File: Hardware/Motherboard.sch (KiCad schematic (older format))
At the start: 1 part

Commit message: [Hardware] Added RTC battery and Adafruit BME680 board.
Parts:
- U1: renamed from U?; footprint (none) -> Package_SO:SOIC-28W_7.5x17.9mm_P1.27mm
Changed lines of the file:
@@
 EESchema Schematic File Version 4
+LIBS:Motherboard-cache
 EELAYER 30 0
 EELAYER END
@@
 $EndDescr
 $Comp
-L PIC18F23K22:PIC18F23K22 U?
+L PIC18F23K22:PIC18F23K22 U1
 U 1 1 5E7A8D16
 P 6300 3950
-F 0 "U?" H 6300 5320 50  0000 C CNN
+F 0 "U1" H 6300 5320 50  0000 C CNN
 F 1 "PIC18F23K22" H 6300 5229 50  0000 C CNN
-F 2 "" H 6300 3950 50  0001 C CNN
+F 2 "Package_SO:SOIC-28W_7.5x17.9mm_P1.27mm" H 6300 3950 50  0001 C CNN
 F 3 "" H 6300 3950 50  0001 C CNN
 	1    6300 3950

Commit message: [Hardware] Replaced PIC18F26K22 microcontroller by PIC18F46K22 to have more pins.
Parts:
- removed U1: PIC18F23K22, Package_SO:SOIC-28W_7.5x17.9mm_P1.27mm, symbol PIC18F23K22:PIC18F23K22
- added C4: 100n, Capacitor_SMD:C_1206_3216Metric_Pad1.42x1.75mm_HandSolder, symbol Device:C
- added J2: Conn_01x05_Male, Connector_PinHeader_2.54mm:PinHeader_1x05_P2.54mm_Horizontal, symbol Connector:Conn_01x05_Male
- added R3: 10K, Resistor_SMD:R_1206_3216Metric_Pad1.42x1.75mm_HandSolder, symbol Device:R
- added R4: 220, Resistor_SMD:R_1206_3216Metric_Pad1.42x1.75mm_HandSolder, symbol Device:R
- added U?: PIC18F46K22-xPT, Package_QFP:TQFP-44_10x10mm_P0.8mm, symbol MCU_Microchip_PIC18:PIC18F46K22-xPT
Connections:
- net labels added: +5V, GND, RE3
- wire segments 0 -> 16
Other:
- note added: "PICkit 3 standard pinout\nwithout LVP pin"
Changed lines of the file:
@@
 Comment4 ""
 $EndDescr
-$Comp
-L PIC18F23K22:PIC18F23K22 U1
-U 1 1 5E7A8D16
-P 6300 3950
-F 0 "U1" H 6300 5320 50  0000 C CNN
-F 1 "PIC18F23K22" H 6300 5229 50  0000 C CNN
-F 2 "Package_SO:SOIC-28W_7.5x17.9mm_P1.27mm" H 6300 3950 50  0001 C CNN
-F 3 "" H 6300 3950 50  0001 C CNN
-	1    6300 3950
-	1    0    0    -1
-$EndComp
 $Sheet
-S 1000 3000 1500 1500
+S 1000 3050 1500 1500
 U 5E7AB2A0
 F0 "FTDI" 50
@@
 F6 "BME680_SDI" I R 5950 1750 50
 F7 "BME680_CS" I R 5950 1850 50
+F8 "RTC_1HZ" O R 5950 1150 50
 $EndSheet
+$Comp
+L Connector:Conn_01x05_Male J2
+U 1 1 5E7B1C5C
+P 8900 4950
+F 0 "J2" H 9100 5250 50  0000 R CNN
+F 1 "Conn_01x05_Male" H 9100 5350 50  0000 R CNN
+F 2 "Connector_PinHeader_2.54mm:PinHeader_1x05_P2.54mm_Horizontal" H 8900 4950 50  0001 C CNN
+F 3 "~" H 8900 4950 50  0001 C CNN
+	1    8900 4950
+	-1   0    0    1
+$EndComp
+Text Notes 8950 5000 0    50   ~ 0
+PICkit 3 standard pinout\nwithout LVP pin
+$Comp
+L Device:C C4
+U 1 1 5E7B4EF8
+P 7800 5850
+F 0 "C4" H 7915 5987 50  0000 L CNN
+F 1 "100n" H 7915 5896 50  0000 L CNN
+F 2 "Capacitor_SMD:C_1206_3216Metric_Pad1.42x1.75mm_HandSolder" H 7838 5700 50  0001 C CNN
+F 3 "~" H 7800 5850 50  0001 C CNN
+F 4 "25V" H 7915 5805 50  0000 L CNN "Champ4"
+F 5 "X7R" H 7915 5714 50  0000 L CNN "Champ5"
+	1    7800 5850
+	1    0    0    -1
+$EndComp
+$Comp
+L Device:R R?
+U 1 1 5E7BB06E
+P 7550 5650
+AR Path="/5E7ACE5B/5E7BB06E" Ref="R?"  Part="1"
+AR Path="/5E7BB06E" Ref="R4"  Part="1"
+F 0 "R4" V 7343 5650 50  0000 C CNN
+F 1 "220" V 7434 5650 50  0000 C CNN
+F 2 "Resistor_SMD:R_1206_3216Metric_Pad1.42x1.75mm_HandSolder" V 7480 5650 50  0001 C CNN
+F 3 "~" H 7550 5650 50  0001 C CNN
+	1    7550 5650
+	0    1    1    0
+$EndComp
+$Comp
+L power:+5V #PWR0111
+U 1 1 5E7BC5F8
+P 7800 5200
+F 0 "#PWR0111" H 7800 5050 50  0001 C CNN
+F 1 "+5V" H 7815 5373 50  0000 C CNN
+F 2 "" H 7800 5200 50  0001 C CNN
+F 3 "" H 7800 5200 50  0001 C CNN
+	1    7800 5200
+	1    0    0    -1
+$EndComp
+$Comp
+L Device:R R?
+U 1 1 5E7BD333
+P 7800 5450
+AR Path="/5E7ACE5B/5E7BD333" Ref="R?"  Part="1"
+AR Path="/5E7BD333" Ref="R3"  Part="1"
+F 0 "R3" H 7730 5404 50  0000 R CNN
+F 1 "10K" H 7730 5495 50  0000 R CNN
+F 2 "Resistor_SMD:R_1206_3216Metric_Pad1.42x1.75mm_HandSolder" V 7730 5450 50  0001 C CNN
+F 3 "~" H 7800 5450 50  0001 C CNN
+	1    7800 5450
+	-1   0    0    1
+$EndComp
+Wire Wire Line
+	8700 4750 7100 4750
+Wire Wire Line
+	7100 4850 8700 4850
+$Comp
+L power:GND #PWR0112
+U 1 1 5E7C6C3E
+P 7800 6100
+F 0 "#PWR0112" H 7800 5850 50  0001 C CNN
+F 1 "GND" H 7805 5927 50  0000 C CNN
+F 2 "" H 7800 6100 50  0001 C CNN
+F 3 "" H 7800 6100 50  0001 C CNN
+	1    7800 6100
+	1    0    0    -1
+$EndComp
+$Comp
+L power:GND #PWR0113
+U 1 1 5E7CC116
+P 8150 5100
+F 0 "#PWR0113" H 8150 4850 50  0001 C CNN
+F 1 "GND" H 8155 4927 50  0000 C CNN
+F 2 "" H 8150 5100 50  0001 C CNN
+F 3 "" H 8150 5100 50  0001 C CNN
+	1    8150 5100
+	1    0    0    -1
+$EndComp
+$Comp
+L power:+5V #PWR0114
+U 1 1 5E7CC521
+P 8350 5100
+F 0 "#PWR0114" H 8350 4950 50  0001 C CNN
+F 1 "+5V" H 8365 5273 50  0000 C CNN
+F 2 "" H 8350 5100 50  0001 C CNN
+F 3 "" H 8350 5100 50  0001 C CNN
+	1    8350 5100
+	-1   0    0    1
+$EndComp
+Wire Wire Line
+	8700 5150 8600 5150
+Wire Wire Line
+	8600 5150 8600 5650
+Wire Wire Line
+	8700 5050 8350 5050
+Wire Wire Line
+	8350 5050 8350 5100
+Wire Wire Line
+	8700 4950 8150 4950
+Wire Wire Line
+	8150 4950 8150 5100
+Wire Wire Line
+	7700 5650 7800 5650
+Wire Wire Line
+	7800 5650 7800 5600
+Connection ~ 7800 5650
+Wire Wire Line
+	7800 5650 8600 5650
+Wire Wire Line
+	7800 5650 7800 5700
+Wire Wire Line
+	7800 5300 7800 5200
+Wire Wire Line
+	7800 6000 7800 6100
+$Comp
+L MCU_Microchip_PIC18:PIC18F46K22-xPT U?
+U 1 1 5E7EF1E1
+P 5800 3850
+F 0 "U?" H 5750 5231 50  0000 C CNN
+F 1 "PIC18F46K22-xPT" H 5750 5140 50  0000 C CNN
+F 2 "Package_QFP:TQFP-44_10x10mm_P0.8mm" H 5650 3650 50  0001 C CIN
+F 3 "http://ww1.microchip.com/downloads/en/DeviceDoc/40001412G.pdf" H 5750 3450 50  0001 C CNN
+	1    5800 3850
+	1    0    0    -1
+$EndComp
+Wire Wire Line
+	7400 5650 7050 5650
+Text Label 7050 5650 0    50   ~ 0
+RE3
+Wire Wire Line
+	7100 2850 7500 2850
+Text Label 7500 2850 2    50   ~ 0
+RE3
 $EndSCHEMATC

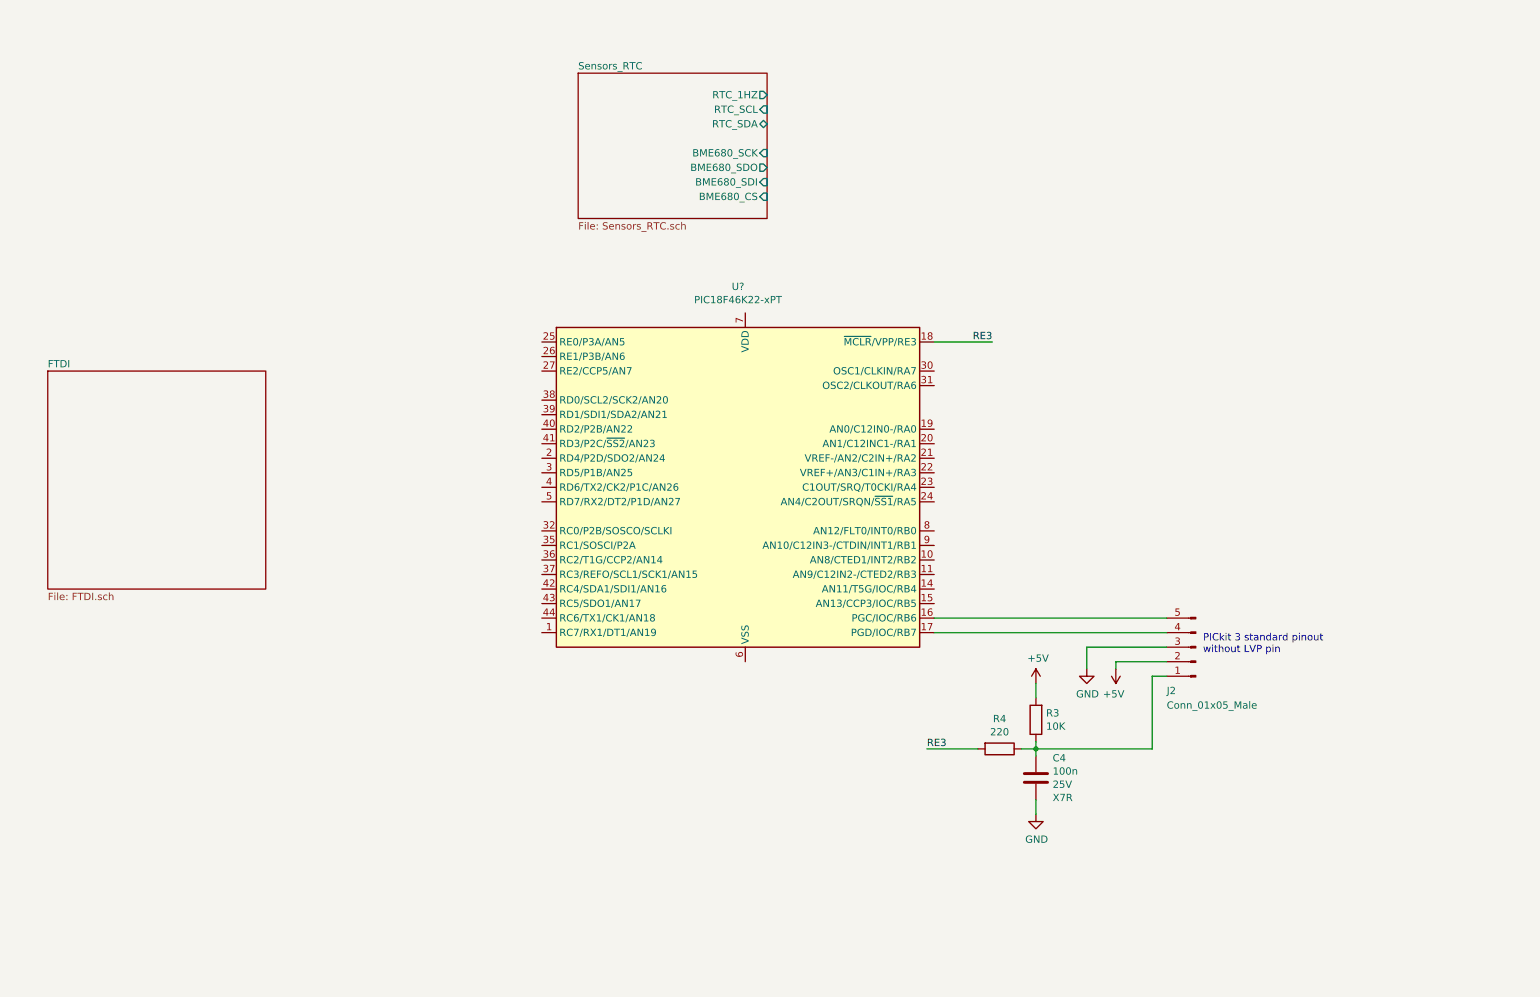
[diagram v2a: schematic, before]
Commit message: [Hardware] Added display support.
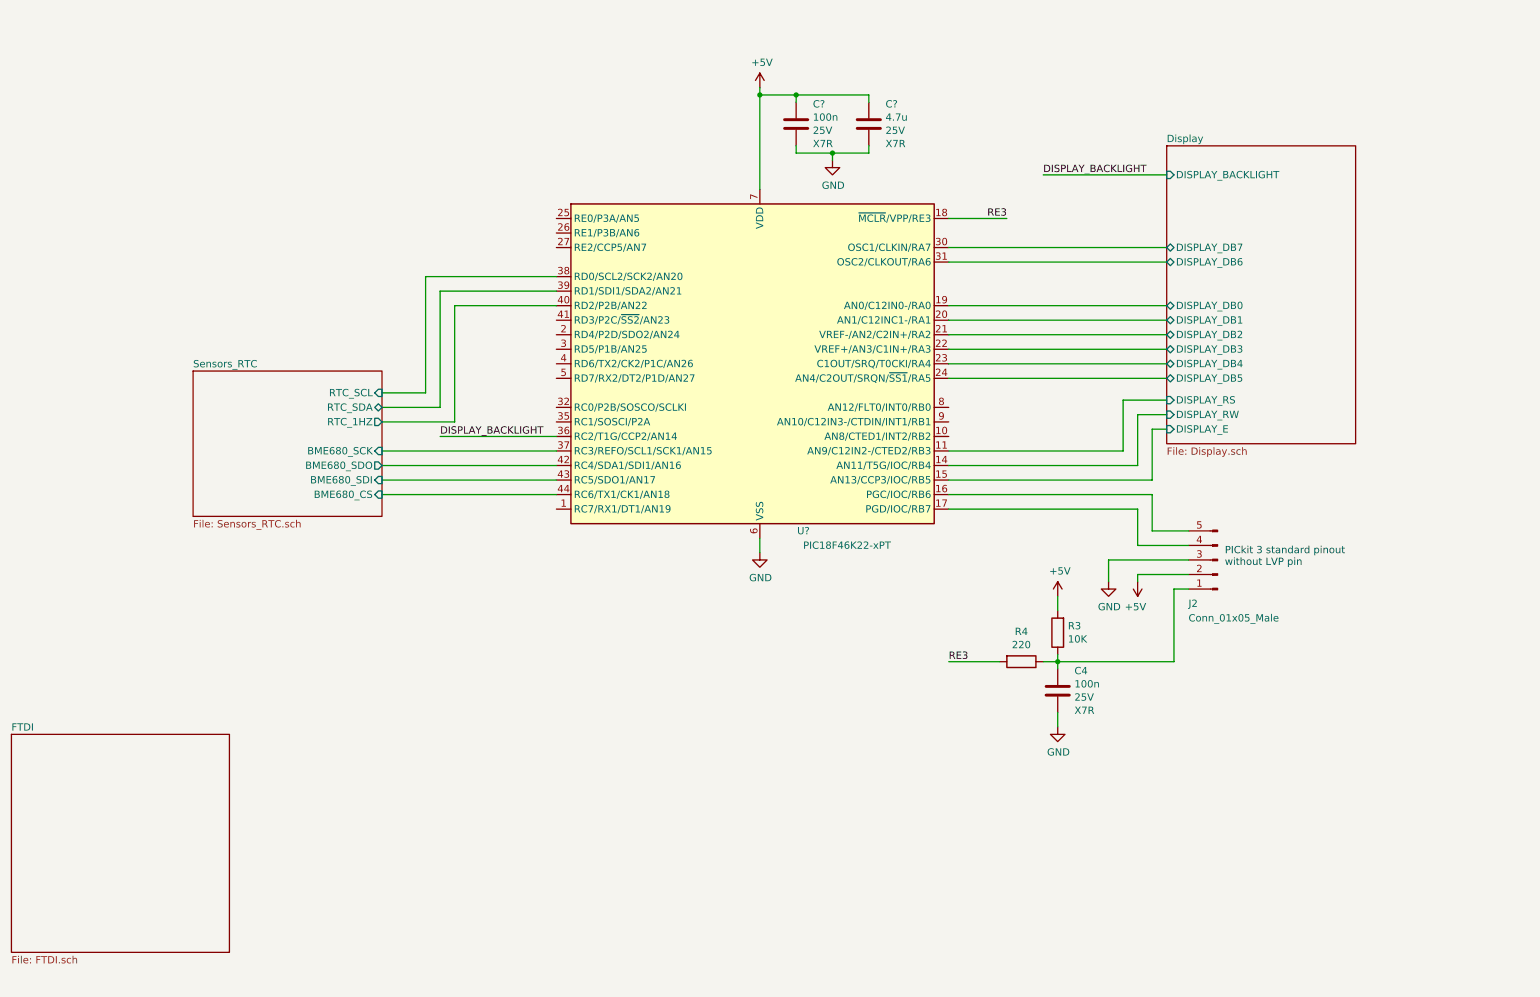
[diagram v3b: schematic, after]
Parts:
- added C?: 100n, Capacitor_SMD:C_1206_3216Metric_Pad1.42x1.75mm_HandSolder, symbol Device:C
- added C?: 4.7u, Capacitor_SMD:C_1206_3216Metric_Pad1.42x1.75mm_HandSolder, symbol Device:C
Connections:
- net +5V: now also U?.28 (VDD), U?.7 (VDD), C?.1, C?.1
- net GND: now also U?.29 (VSS), U?.6 (VSS), C?.2, C?.2
- net Sensors_RTC/BME680_CS: now also U?.44 (RC6/TX1/CK1/AN18)
- net Sensors_RTC/BME680_SCK: now also U?.37 (RC3/REFO/SCL1/SCK1/AN15)
- net Sensors_RTC/BME680_SDI: now also U?.43 (RC5/SDO1/AN17)
- net Sensors_RTC/BME680_SDO: now also U?.42 (RC4/SDA1/SDI1/AN16)
- net Sensors_RTC/RTC_1HZ: now also U?.40 (RD2/P2B/AN22)
- net Sensors_RTC/RTC_SCL: now also U?.38 (RD0/SCL2/SCK2/AN20)
- net Sensors_RTC/RTC_SDA: now also U?.39 (RD1/SDI1/SDA2/AN21)
- net Display/DISPLAY_RS: now reaches U?.11 (AN9/C12IN2-/CTED2/RB3)
- net Display/DISPLAY_RW: now reaches U?.14 (AN11/T5G/IOC/RB4)
- net Display/DISPLAY_E: now reaches U?.15 (AN13/CCP3/IOC/RB5)
- net Display/DISPLAY_DB0: now reaches U?.19 (AN0/C12IN0-/RA0)
- net Display/DISPLAY_DB1: now reaches U?.20 (AN1/C12INC1-/RA1)
- net Display/DISPLAY_DB2: now reaches U?.21 (VREF-/AN2/C2IN+/RA2)
- net Display/DISPLAY_DB3: now reaches U?.22 (VREF+/AN3/C1IN+/RA3)
- net Display/DISPLAY_DB4: now reaches U?.23 (C1OUT/SRQ/T0CKI/RA4)
- net Display/DISPLAY_DB5: now reaches U?.24 (AN4/C2OUT/SRQN/~SS1~/RA5)
- net Display/DISPLAY_DB7: now reaches U?.30 (OSC1/CLKIN/RA7)
- net Display/DISPLAY_DB6: now reaches U?.31 (OSC2/CLKOUT/RA6)
- net DISPLAY_BACKLIGHT: now reaches U?.36 (RC2/T1G/CCP2/AN14)
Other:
- moved on the sheet: C4, J2, R3, R4, U?

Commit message: [Hardware] Added buttons.
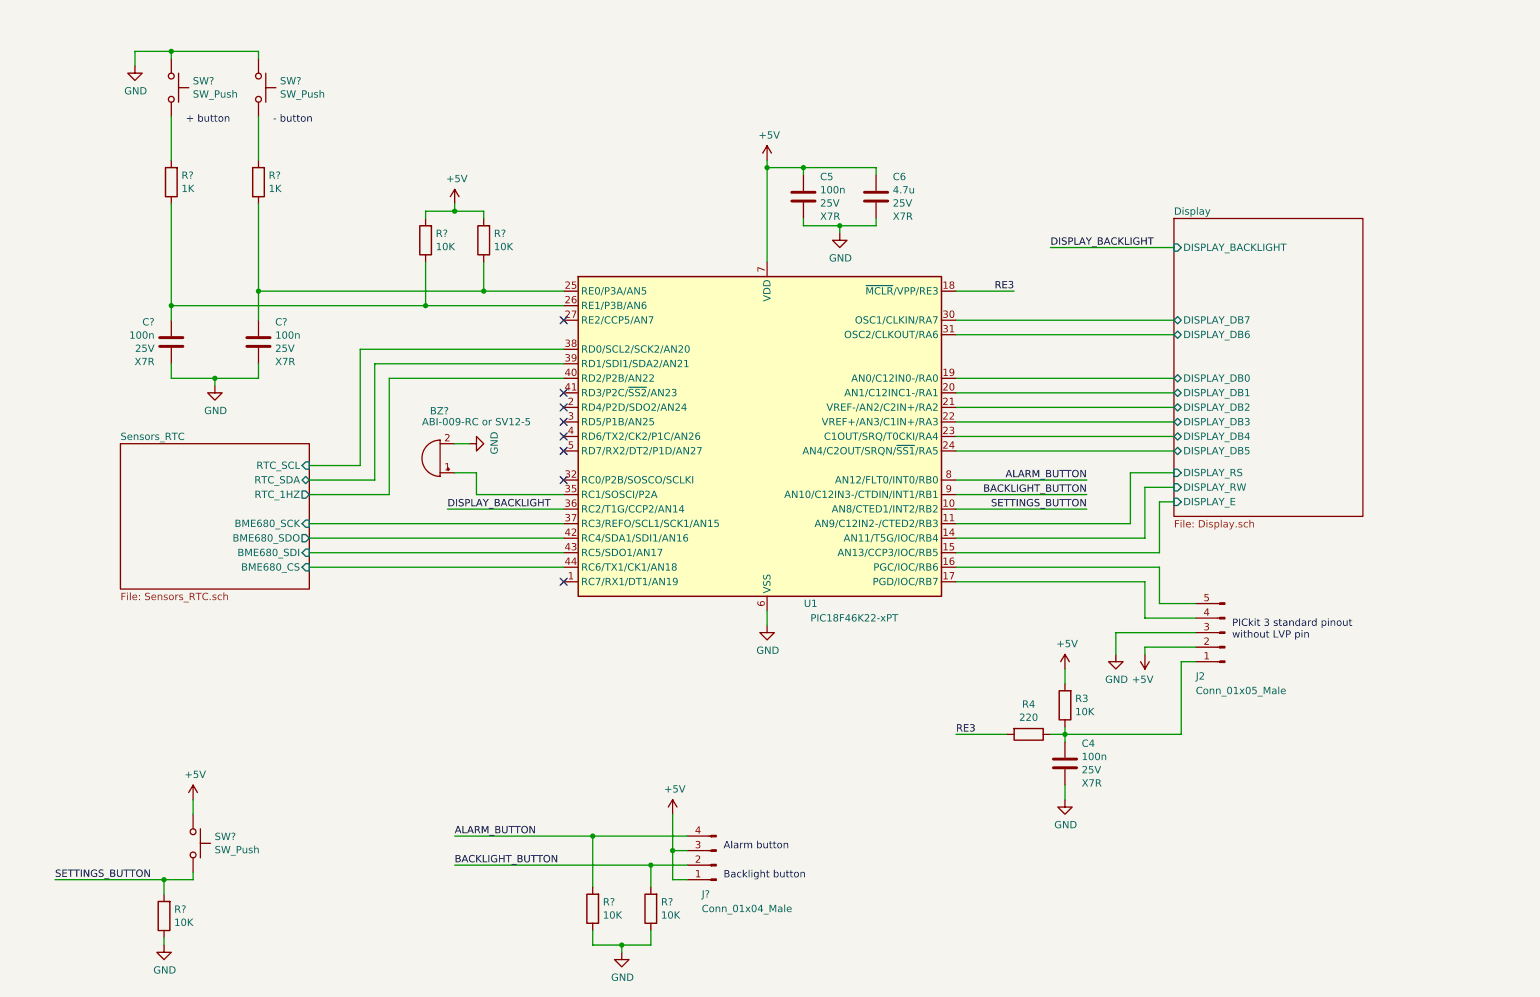
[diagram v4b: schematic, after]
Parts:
- added BZ?: ABI-009-RC or SV12-5, Buzzer_Beeper:MagneticBuzzer_ProSignal_ABI-009-RC, symbol Device:Buzzer
- added C? (x2): 100n, Capacitor_SMD:C_1206_3216Metric_Pad1.42x1.75mm_HandSolder, symbol Device:C
- added J?: Conn_01x04_Male, symbol Connector:Conn_01x04_Male
- added R? (x5): 10K, Resistor_SMD:R_1206_3216Metric_Pad1.42x1.75mm_HandSolder, symbol Device:R
- added R? (x2): 1K, Resistor_SMD:R_1206_3216Metric_Pad1.42x1.75mm_HandSolder, symbol Device:R
- added SW? (x3): SW_Push, symbol Switch:SW_Push
- gave numbers to parts that had none: 3
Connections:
- net +5V: now also J?.1 (Pin_1), J?.3 (Pin_3), R?.2, R?.2, SW?.1
- net GND: now also BZ?.2 (+), C?.1, C?.1, R?.1, R?.1, R?.1, SW?.1, SW?.1
- net SETTINGS_BUTTON: now reaches U1.10 (AN8/CTED1/INT2/RB2)
- net SETTINGS_BUTTON: now also R?.2, SW?.2
- net at U1.25 (RE0/P3A/AN5): now also C?.2, R?.1, R?.1
- net at U1.26 (RE1/P3B/AN6): now also C?.2, R?.1, R?.1
- net at U1.35 (RC1/SOSCI/P2A): now also BZ?.1 (-)
- net ALARM_BUTTON: now reaches U1.8 (AN12/FLT0/INT0/RB0)
- net ALARM_BUTTON: now also J?.4 (Pin_4), R?.2
- net BACKLIGHT_BUTTON: now reaches U1.9 (AN10/C12IN3-/CTDIN/INT1/RB1)
- net BACKLIGHT_BUTTON: now also J?.2 (Pin_2), R?.2
- new net: R?.2, SW?.2 (x2)
- no-connect marks 0 -> 8
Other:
- note added: "+ button"
- note added: "- button"
- note added: "Alarm button"
- note added: "Backlight button"
- moved on the sheet: C4, C5, C6, J2, R3, R4, U1

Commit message: [Hardware] Added simpler buttons debouncing and also added debouncing to buttons that trigger an interrupt.
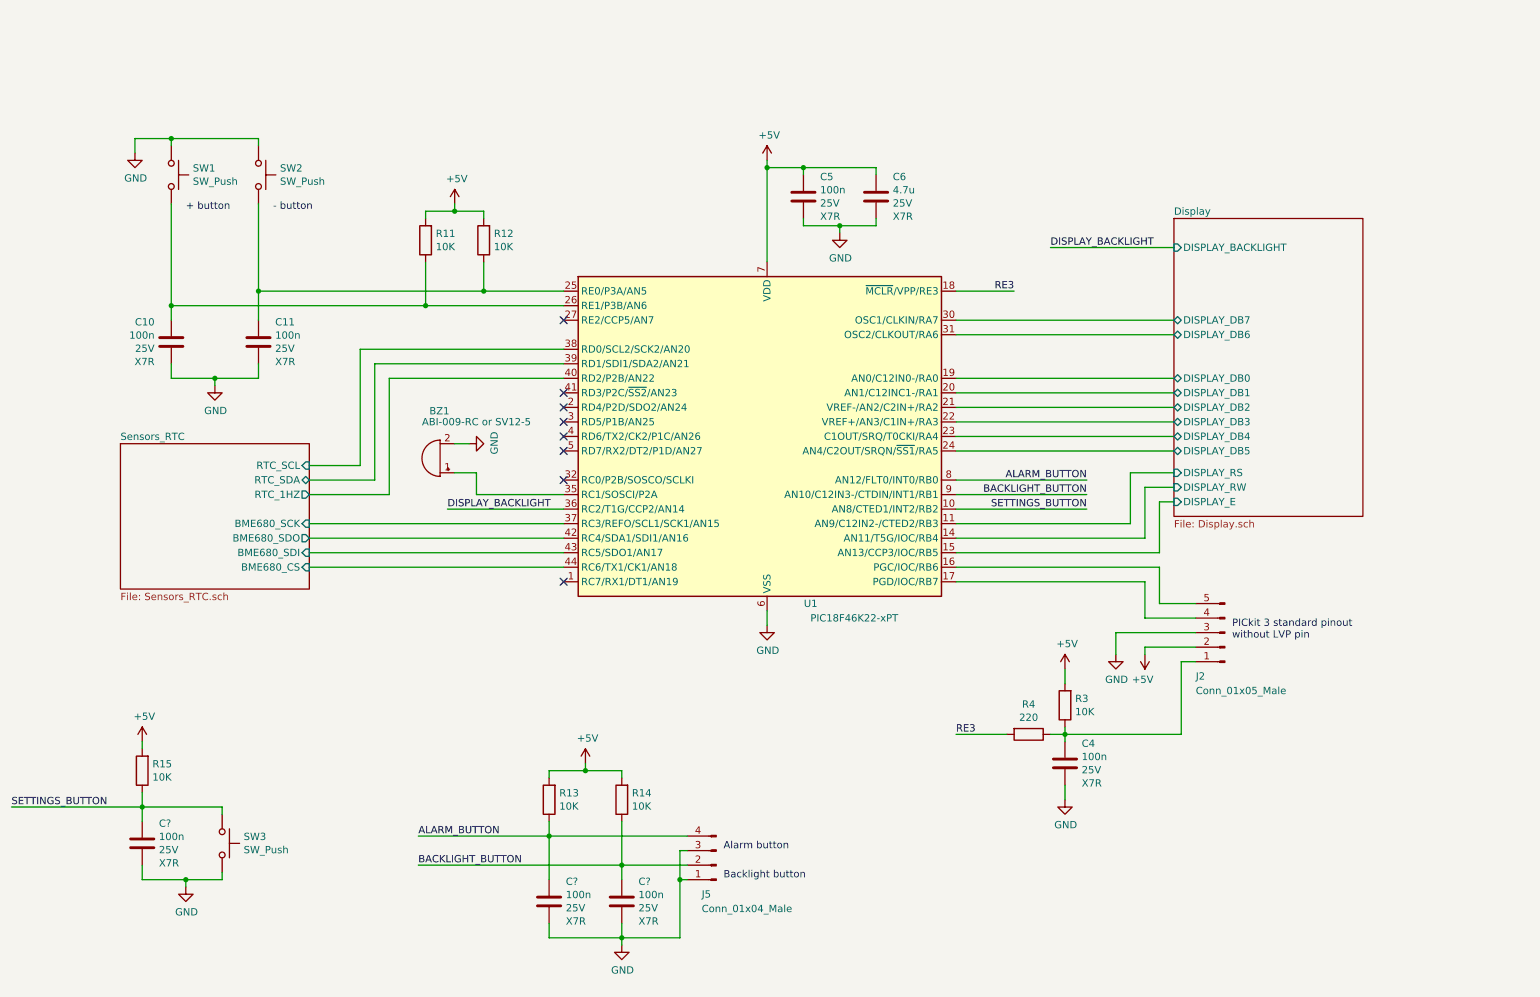
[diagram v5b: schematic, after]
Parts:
- removed R? (x2): 1K, Resistor_SMD:R_1206_3216Metric_Pad1.42x1.75mm_HandSolder, symbol Device:R
- added C? (x3): 100n, Capacitor_SMD:C_1206_3216Metric_Pad1.42x1.75mm_HandSolder, symbol Device:C
- gave numbers to parts that had none: 12
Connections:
- net +5V: now also R13.2, R14.2, R15.2; no longer J5.1 (Pin_1), J5.3 (Pin_3), SW3.1
- net ALARM_BUTTON: now also R13.1, C?.2; no longer R13.2
- net BACKLIGHT_BUTTON: now also R14.1, C?.2; no longer R14.2
- net GND: now also J5.1 (Pin_1), J5.3 (Pin_3), SW3.2, C?.1, C?.1, C?.1; no longer R13.1, R14.1, R15.1
- net SETTINGS_BUTTON: now also R15.1, SW3.1, C?.2; no longer R15.2, SW3.2
- net at C11.2, R12.1, U1.25 (RE0/P3A/AN5): now also SW2.2
- net at C10.2, R11.1, U1.26 (RE1/P3B/AN6): now also SW1.2
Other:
- moved on the sheet: R13, R14, R15, SW1, SW2, SW3
